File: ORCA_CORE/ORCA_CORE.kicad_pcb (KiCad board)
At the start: 2 copper layers, 69.8 x 41.9 mm, 176 parts, among them J1 data_line_power, J10 Raspberry_Pi_2_3, J11 I2C, J12 I2C, J13 6Vout, J14 5Vout, J15 Conn_01x05_Pin, J16 Conn_01x05_Pin, J17 Vin_motor, J18 data_line_power, J19 +5Vout_cpu, J2 I2C_power, J20 5Vout, J3 Vout_motor, J4 emergence, J5 Vin_batt, J6 Vin_ex, J7 Vout_power2usp, J8 Vin_power2usp, J9 +5Vout_cpu, P1 USB_C_Plug_USB2.0, Q1 TJ60S04M3L, Q2 BSS138, Q3 BSS138, Q4 IRLML6402, Q5 TJ60S04M3L, Q6 BSS138, Q7 BSS138, U1 LTC2301IMS, U10 HY2112, U11 AP64502, U12 TPS61230A__board, U13 FT230XS, U14 BNO055, U15 NJM78055DL1, U2 NJM78055DL1, U3 CN3058E, U4 RH1B-UDC6V, U5 TPH11006NL, U6 TPH11006NL, U7 NJW4860, U8 AZ1117-3.3, U9 FS8205

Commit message: plate power and usp
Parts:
- removed H7, H8: Hole_usp, MountingHole:MountingHole_3.2mm_M3
- added C51: 4.7u, Capacitor_SMD:C_0603_1608Metric_Pad1.08x0.95mm_HandSolder, B.Cu at (197.5, -40.9)
- added J21: Conn_01x02, Battery:BatteryHolder_1xAA_code, F.Cu at (162.9, -53.8)
- added ORCA_CORE: LOGO, Logo:ORCA_logo, F.Cu at (69.8, -38.7)
- added ORCA_CORE: LOGO, Logo:ORCA_logo, F.Cu at (164.7, -41.7)
- added Q8: BSS138, Package_TO_SOT_SMD:SOT-23, F.Cu at (-70.5, 60.0)
- added R5: 0, Resistor_SMD:R_0603_1608Metric_Pad0.98x0.95mm_HandSolder, F.Cu at (221.6, -43.6)
- added R6: 2.2k, Resistor_SMD:R_0603_1608Metric_Pad0.98x0.95mm_HandSolder, F.Cu at (-70.8, 63.5)
- C24, C25, C26, C27, C28, C29, C30, C31, C32, C33, C34, C35, C41, D13, D17, Q5, R21, R22, R23, R24, R25, R26, R27, R28, R29, R30, R31, R32, R33, U10, U11, U3, U9: moved to B.Cu
- J19: value +5Vout_cpu -> +5Vin_cpu
- L1: footprint Inductor_SMD:L_12x12mm_H8mm -> Inductor_SMD:L_12x12mm_H8mm_withmodel
- P1: footprint Connector_USB:USB_C_Receptacle_HCTL_HC-TYPE-C-16P-01A -> Connector_USB:USB_C_Receptacle_HCTL_HC-TYPE-C-16P-01A_withmodel
- R34: value 0 -> 2.2k
- moved U10 350.3 mm to (214.4, -58.2)
- moved U9 342.0 mm to (214.4, -53.5), turned to 180 degrees
- moved U3 337.7 mm to (165.7, -58.6), turned to 180 degrees
- moved R27 336.5 mm to (208.1, -48.1), turned to 180 degrees
- moved D18 335.1 mm to (201.3, -40.5)
- moved R30 334.8 mm to (208.5, -58.2), turned to -90 degrees
- moved H6 334.4 mm to (223.3, -59.2)
- moved D17 333.8 mm to (191.4, -46.2), turned to 180 degrees
- moved R26 333.3 mm to (211.2, -45.6), turned to 180 degrees
- moved C35 333.0 mm to (206.0, -58.2), turned to -90 degrees
- moved C25 332.4 mm to (165.7, -55.1)
- moved R25 329.4 mm to (211.2, -43.7), turned to 180 degrees
- moved R29 328.3 mm to (208.5, -53.5), turned to -90 degrees
- moved C29 328.2 mm to (207.7, -44.6), turned to -90 degrees
- moved C39 327.4 mm to (199.3, -31.7), turned to 90 degrees
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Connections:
- C25 pad 1: bat+ -> batt+
- C31 pad 1: GND -> GND1
- C31 pad 2: /usp/Vout -> reg_down_out
- C32 pad 1: GND -> GND1
- C32 pad 2: /usp/Vout -> reg_down_out
- C33 pad 1: GND -> GND1
- C33 pad 2: /usp/Vout -> reg_down_out
- C34 pad 1: GND -> GND1
- C34 pad 2: /usp/Vout -> reg_down_out
- C39 pad 1: GND -> reg_down_out
- C39 pad 2: /usp/Vout -> GND1
- C40 pad 2: GND -> GND1
- C41 pad 2: reg_up_out -> reg_down
- C42 pad 2: reg_up_out -> reg_down
- C43 pad 2: reg_up_out -> reg_down
- C44 pad 2: GND -> GND1
- C45 pad 2: GND -> GND1
- D16 pad 1: /usp/Vout -> reg_down_out
- D18 pad 1: /usp/Vout -> reg_down
- D19 pad 1: GND -> GND1
- D23 pad 1: GND -> GND1
- D24 pad 3: GND -> GND1
- D24 pad 4: full_color_led -> full_color_led_5V
- J10 pad 14: GND -> GND1
- J10 pad 20: GND -> GND1
- J10 pad 22: full_color_led -> full_color_led_3V3
- J10 pad 25: GND -> GND1
- J10 pad 30: GND -> GND1
- J10 pad 34: GND -> GND1
- J10 pad 39: GND -> GND1
- J10 pad 6: GND -> GND1
- J10 pad 9: GND -> GND1
- J14 pad 1: GND -> GND1
- J19 pad 1: GND -> GND1
- J9 pad 1: GND -> GND1
- J9 pad 2: /usp/Vout -> reg_down_out
- P1 pad A1: GND -> GND1
- P1 pad A12: GND -> GND1
- P1 pad B1: GND -> GND1
- P1 pad B12: GND -> GND1
- P1 pad S1: GND -> GND1
- R34 pad 1: GND -> +5V_cpu
- R34 pad 2: GND -> full_color_led_5V
- R39 pad 1: GND -> GND1
- U13 pad 13: GND -> GND1
- U13 pad 5: GND -> GND1
- U14 pad 2: GND -> GND1
- U14 pad 7: GND -> GND1
- U3 pad 5: bat+ -> batt+
- U3 pad 8: bat+ -> batt+
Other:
- board size 69.8 x 41.9 mm -> 169.9 x 43 mm
- board text added: "3V3"
- board text added: "5Vout"
- board text added: "I2C"
- board text added: "SCL"
- board text added: "SDA"
- board text added: "Vin"
- board text added: "batt"
- board text added: "battery"
- board text added: "charge"
- board text added: "data line"
- board text added: "emerge_detector"
- board text added: "emerge_order"
- board text added: "enable"
- board text added: "external"
- board text added: "full"
- board text added: "motor"
- board text added: "power board v1 2025/02/19"
- board text added: "power_checker"
- board text added: "usp"
- board text added: "usp board v1 2025/02/19"

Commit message: plate all parts
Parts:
- removed H11, H12: Hole_cup, MountingHole:MountingHole_3.2mm_M3
- removed J14: 5Vout, Conn:power_pad
- added ORCA_CORE: LOGO, Logo:ORCA_logo, F.Cu at (106.0, 46.4)
- added R47: 2.2k, Resistor_SMD:R_0603_1608Metric_Pad0.98x0.95mm_HandSolder, F.Cu at (118.1, 55.6)
- added R48: 2.2k, Resistor_SMD:R_0603_1608Metric_Pad0.98x0.95mm_HandSolder, F.Cu at (120.7, 55.6)
- added R49: 2.2k, Resistor_SMD:R_0603_1608Metric_Pad0.98x0.95mm_HandSolder, F.Cu at (115.6, 55.6)
- added R50: 2.2k, Resistor_SMD:R_0603_1608Metric_Pad0.98x0.95mm_HandSolder, B.Cu at (124.2, 153.3)
- C40, C44, C45, C46, C47, C48, C49, C50, D22, D25, Q6, Q7, Q8, R34, R37, R38, R39, R40, R41, R42, R43, R44, R45, R46, R6, U13, U15: moved to B.Cu
- J10: footprint Connector_PinSocket_2.54mm:PinSocket_2x20_P2.54mm_Horizontal -> cpu:raspberrypi_Zero_W_Vertical
- moved J10 273.3 mm to (153.8, 41.3), turned to -90 degrees
- moved R35 270.6 mm to (156.8, 42.8), turned to -90 degrees
- moved C47 269.4 mm to (154.9, 61.0), turned to 90 degrees
- moved C40 268.9 mm to (154.9, 45.2), turned to -90 degrees
- moved R36 267.6 mm to (156.8, 61.3), turned to 90 degrees
- moved C46 267.0 mm to (152.4, 61.0), turned to 90 degrees
- moved C45 266.2 mm to (152.3, 45.2), turned to -90 degrees
- moved D24 259.7 mm to (148.0, 63.2)
- moved J15 253.2 mm to (152.7, 49.6), turned to -90 degrees
- moved C48 248.7 mm to (157.5, 60.9), turned to 90 degrees
- moved J16 248.6 mm to (152.7, 53.4), turned to -90 degrees
- moved R40 248.5 mm to (138.4, 62.7), turned to -90 degrees
- moved C44 246.8 mm to (157.5, 45.4), turned to -90 degrees
- moved R41 246.6 mm to (137.2, 53.4), turned to -90 degrees
- moved R42 246.5 mm to (137.2, 48.3), turned to 90 degrees
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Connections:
- R41 pad 2: SDA -> SCL
- R42 pad 2: SCL -> SDA
- U14 pad 3: SCL -> SDA
- U14 pad 4: SDA -> SCL
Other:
- board size 169.9 x 43 mm -> 73 x 134.1 mm
- board text added: "12"
- board text added: "13"
- board text added: "16"
- board text added: "17"
- board text added: "18"
- board text added: "19"
- board text added: "20"
- board text added: "21"
- board text added: "26"
- board text added: "27"
- board text added: "Vin_5Vcpu"
- board text added: "cpu board v1 2025/02/19"
- board text added: "emerge sw"
- board text removed: "batt"

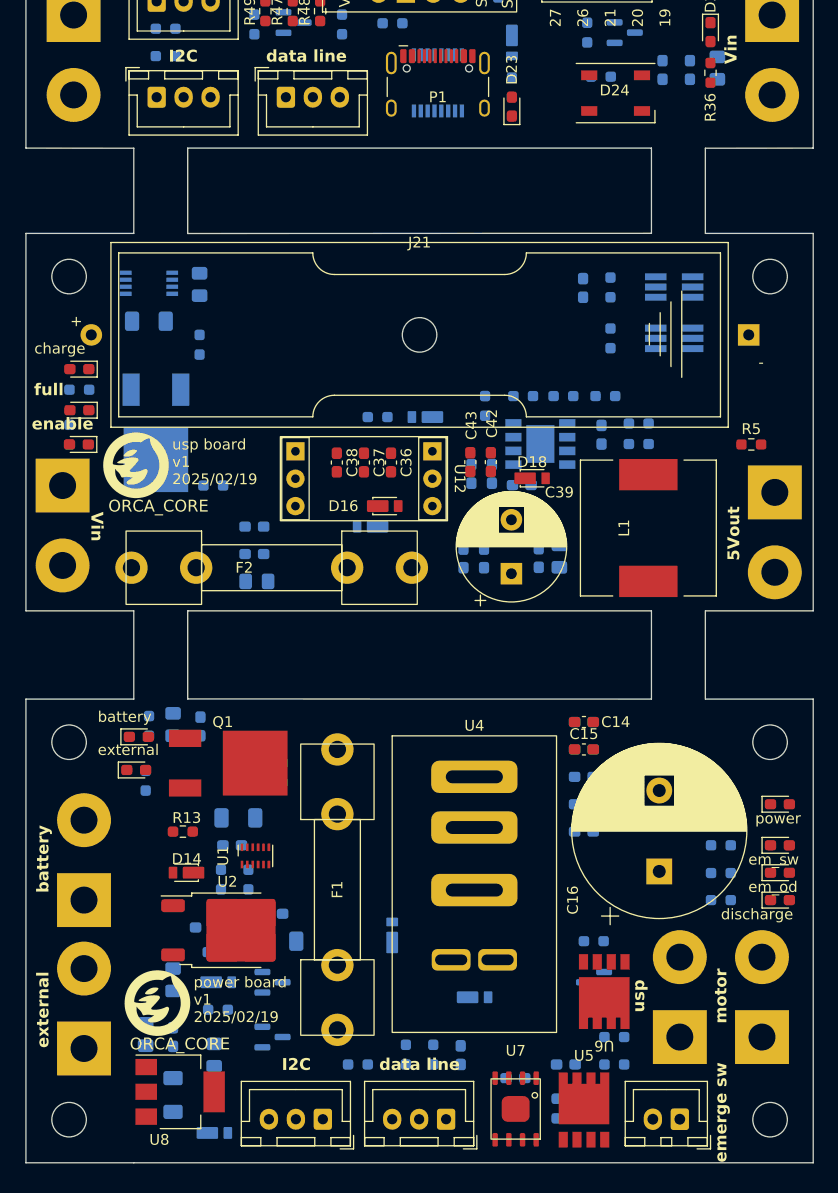
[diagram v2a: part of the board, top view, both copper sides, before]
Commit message: wire and fill power board
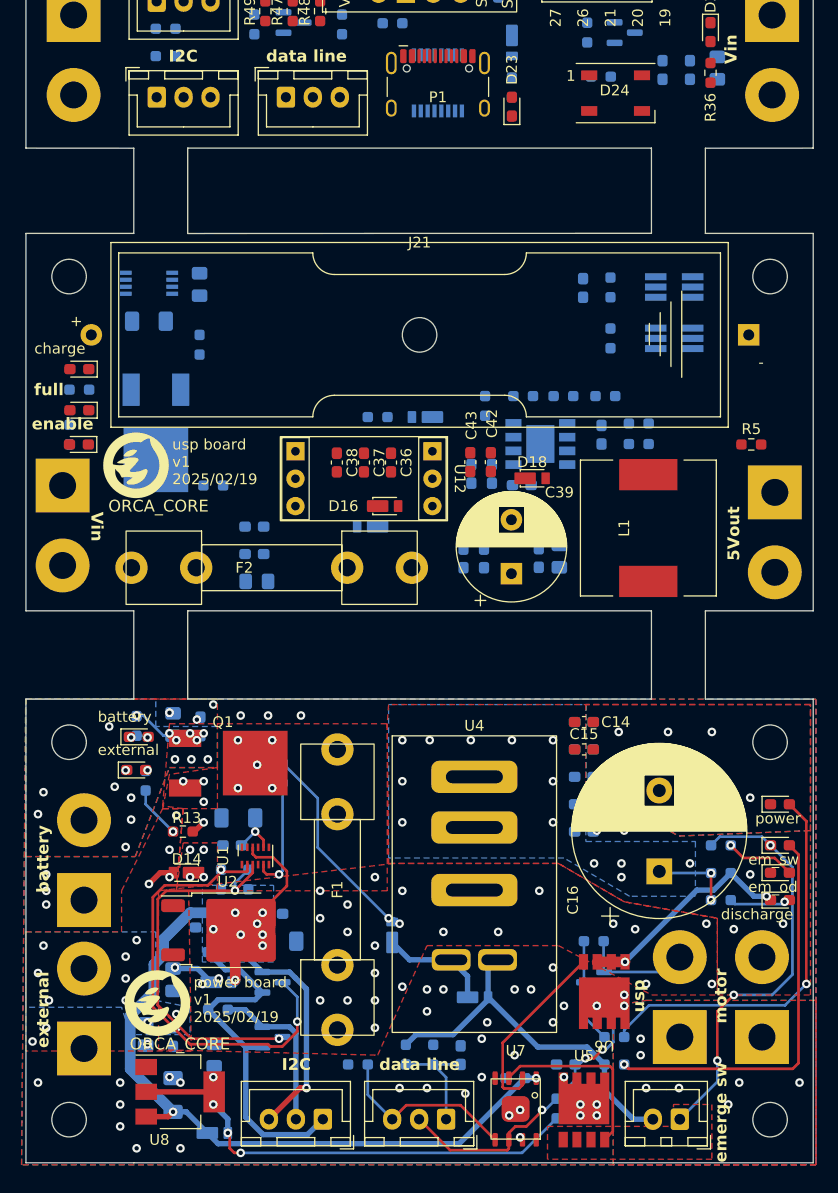
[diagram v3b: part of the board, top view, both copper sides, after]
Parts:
- moved R1 1.15 mm to (103.6, 121.9)
- turned R14 to 0 degrees
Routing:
- net +5V_power: track 0.00 -> 82.1 mm, vias 0 -> 10
- net +3V3_power: track 0.00 -> 46.4 mm, vias 0 -> 4
- net SDA_5V: track 0.00 -> 41.5 mm, vias 0 -> 2
- net Net-(D6-K): track 0.00 -> 38.8 mm, vias 0 -> 3
- net Net-(D6-A): track 0.00 -> 37.1 mm, vias 0 -> 1
- net Net-(D5-A): track 0.00 -> 36.6 mm, vias 0 -> 1
- net SCL_5V: track 0.00 -> 35.8 mm, vias 0 -> 2
- net +6V_power: track 0.00 -> 35.5 mm, vias 0 -> 26
- net Net-(D4-A): track 0.00 -> 34.8 mm
- net VBUS_power: track 0.00 -> 33.7 mm
- net /power/power_checker: track 0.00 -> 30.4 mm, vias 0 -> 3
- net /power/SDA_3V3: track 0.00 -> 22.6 mm, vias 0 -> 1
- net Net-(D8-K): track 0.00 -> 20.5 mm, vias 0 -> 2
- net /power/emerge_order: track 0.00 -> 17.4 mm
- net Net-(U7-OUTA): track 0.00 -> 17.4 mm
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- added copper zone on B.Cu, net +5V_power
- added copper zone on F.Cu, net +6V_power
- added copper zone on In1.Cu, net +6V_power
- added copper zone on B.Cu, net +BATT_power
- added copper zone on F.Cu, net +BATT_power
- added copper zone on In1.Cu, net +BATT_power
- added copper zone on B.Cu, net +VDD_power
- added copper zone on F.Cu, net +VDD_power
- added copper zone on In1.Cu, net +VDD_power
- added copper zone on B.Cu, net /power/Vout_motor
- added copper zone on F.Cu, net /power/Vout_motor
- added copper zone on In1.Cu, net /power/Vout_motor
- added copper zone on B.Cu, net GND
- added copper zone on F.Cu, net GND
- added copper zone on In1.Cu, net GND
- added copper zone on In2.Cu, net GND
- added copper zone on F.Cu, net Net-(D14-K)
- added copper zone on In1.Cu, net Net-(D14-K)
- added copper zone on F.Cu, net Net-(D6-K)
- added copper zone on In2.Cu, net Net-(Q1-G)
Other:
- copper layers 2 -> 4

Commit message: wiring and filling power complete
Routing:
- net GND: track 0.68 -> 9.18 mm, vias 65 -> 75
- net +VDD_power: track 7.53 -> 10.2 mm, vias 17 -> 14
- net Net-(D6-K): track 38.8 -> 41.3 mm
- net Net-(D14-K): track 0.00 -> 2.26 mm
- net Net-(U7-OUTB): track 17.1 -> 16.0 mm, vias 0 -> 2
- net Net-(D5-A): track 36.6 -> 37.5 mm
- net /power/power_checker: track 30.4 -> 31.2 mm
- net +5V_power: track 82.1 -> 82.7 mm, vias 10 -> 12
- net Net-(D8-K): track 20.5 -> 20.7 mm, vias 2 -> 3
- net Net-(D6-A): vias 1 -> 2
- net Net-(D8-A): vias 1 -> 2
- net /power/Vout_motor: vias 18 -> 27
- net +6V_power: vias 26 -> 33
- added copper zone on B.Cu, net +6V_power

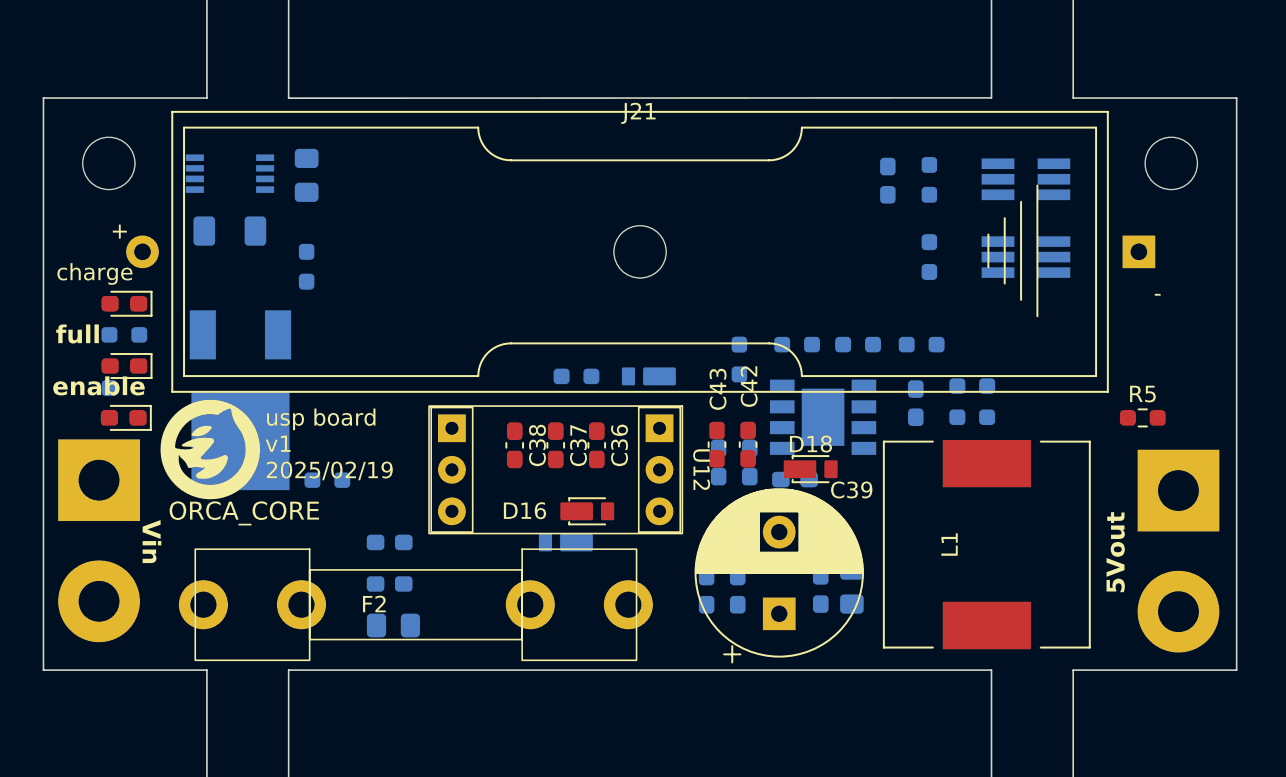
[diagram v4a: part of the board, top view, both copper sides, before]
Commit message: complete wireing and filling usp
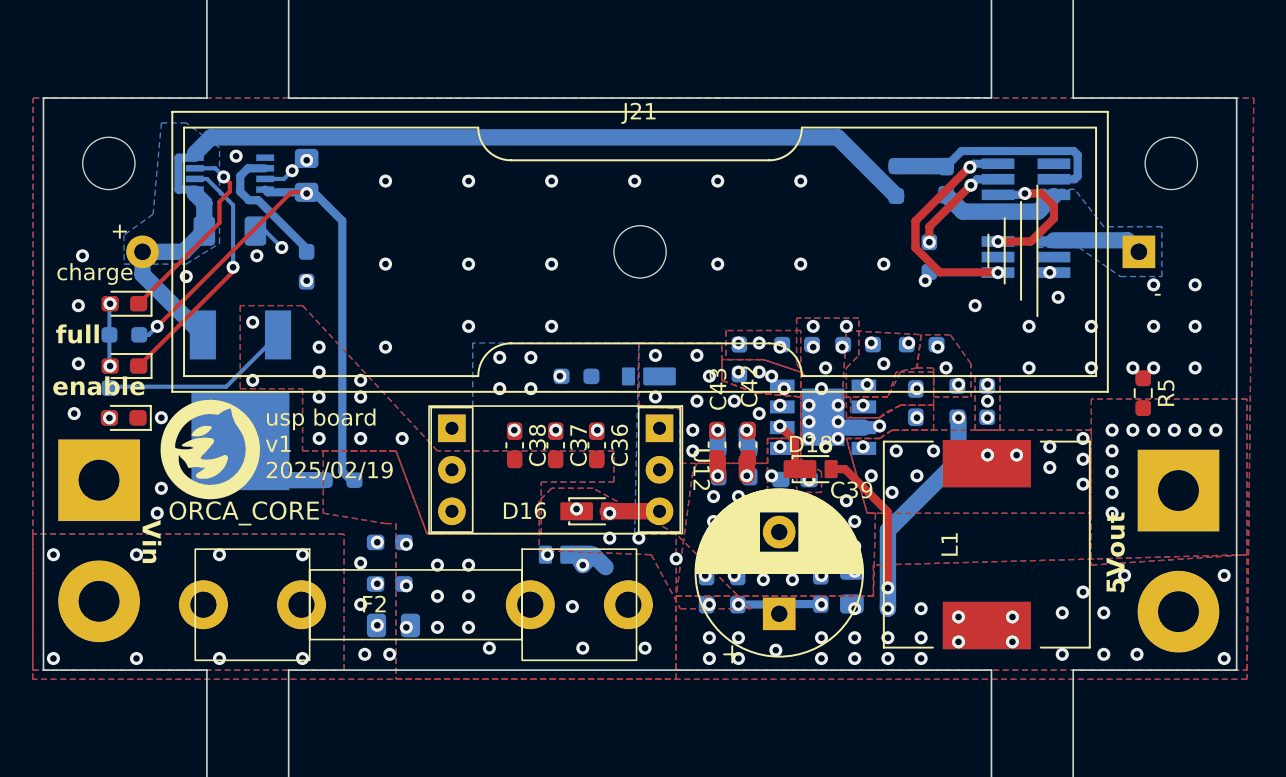
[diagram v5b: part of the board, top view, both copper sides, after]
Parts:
- moved C35 3.56 mm to (148.6, 81.3)
- moved R30 2.03 mm to (145.5, 81.3)
- moved R5 1.51 mm to (160.7, 94.3), turned to -90 degrees
- moved D13 0.75 mm to (125.3, 104.1)
- moved R33 0.74 mm to (111.5, 99.6)
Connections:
- C31 pad 1: GND1 -> GND
- C32 pad 1: GND1 -> GND
- C33 pad 1: GND1 -> GND
- C34 pad 1: GND1 -> GND
- C39 pad 2: GND1 -> GND
- C40 pad 2: GND1 -> GND2
- C44 pad 2: GND1 -> GND2
- C45 pad 2: GND1 -> GND2
- D19 pad 1: GND1 -> GND2
- D23 pad 1: GND1 -> GND2
- D24 pad 3: GND1 -> GND2
- J10 pad 14: GND1 -> GND2
- J10 pad 20: GND1 -> GND2
- J10 pad 25: GND1 -> GND2
- J10 pad 30: GND1 -> GND2
- J10 pad 34: GND1 -> GND2
- J10 pad 39: GND1 -> GND2
- J10 pad 6: GND1 -> GND2
- J10 pad 9: GND1 -> GND2
- J19 pad 1: GND1 -> GND2
- P1 pad A1: GND1 -> GND2
- P1 pad A12: GND1 -> GND2
- P1 pad B1: GND1 -> GND2
- P1 pad B12: GND1 -> GND2
- P1 pad S1: GND1 -> GND2
- R39 pad 1: GND1 -> GND2
- R47 pad 2: GND1 -> GND2
- R48 pad 2: GND1 -> GND2
- R49 pad 2: GND1 -> GND2
- U13 pad 13: GND1 -> GND2
- U13 pad 5: GND1 -> GND2
- U14 pad 2: GND1 -> GND2
- U14 pad 7: GND1 -> GND2
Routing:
- net batt+: track 0.00 -> 62.2 mm
- net reg_down_out: track 0.00 -> 41.2 mm, vias 0 -> 38
- net +VDD_usp: track 0.00 -> 38.4 mm, vias 0 -> 20
- net GND: track 9.18 -> 41.2 mm, vias 75 -> 166
- net Net-(D12-K): track 0.00 -> 15.2 mm, vias 0 -> 1
- net Net-(U10-VDD): track 0.00 -> 14.4 mm
- net Net-(U10-OC): track 0.00 -> 13.8 mm, vias 0 -> 2
- net batt-: track 0.00 -> 12.9 mm
- net Net-(D10-K): track 0.00 -> 12.2 mm, vias 0 -> 1
- net reg_up: track 0.00 -> 11.7 mm, vias 0 -> 10
- net Net-(U10-OD): track 0.00 -> 8.54 mm, vias 0 -> 2
- net Net-(U3-ISET): track 0.00 -> 8.37 mm
- net Net-(U10-CS): track 0.00 -> 6.34 mm, vias 0 -> 2
- net reg_up_out: track 0.00 -> 6.27 mm, vias 0 -> 1
- net Net-(Q5-G): track 0.00 -> 6.14 mm
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- added copper zone on B.Cu, net +VDD_usp
- added copper zone on F.Cu, net +VDD_usp
- added copper zone on In1.Cu, net +VDD_usp
- added copper zone on B.Cu, net /usp/Vin
- added copper zone on F.Cu, net /usp/Vin
- added copper zone on In1.Cu, net /usp/Vin
- added copper zone on In2.Cu, net /usp/Vin
- added copper zone on B.Cu, net GND1
- added copper zone on F.Cu, net GND1
- added copper zone on In1.Cu, net GND1
- added copper zone on In2.Cu, net GND1
- added copper zone on B.Cu, net Net-(R23-Pad2)
- added copper zone on F.Cu, net Net-(R23-Pad2)
- added copper zone on In1.Cu, net Net-(R23-Pad2)
- added copper zone on In2.Cu, net Net-(R23-Pad2)
- added copper zone on B.Cu, net Net-(R25-Pad1)
- added copper zone on F.Cu, net Net-(R25-Pad1)
- added copper zone on In1.Cu, net Net-(R25-Pad1)
- added copper zone on In2.Cu, net Net-(R25-Pad1)
- added copper zone on B.Cu, net Net-(R26-Pad2)
- added copper zone on F.Cu, net Net-(R26-Pad2)
- added copper zone on In1.Cu, net Net-(R26-Pad2)
- added copper zone on In2.Cu, net Net-(R26-Pad2)
- added copper zone on B.Cu, net Net-(U11-BST)
- added copper zone on F.Cu, net Net-(U11-BST)
- added copper zone on In1.Cu, net Net-(U11-BST)
- added copper zone on In2.Cu, net Net-(U11-BST)
- added copper zone on B.Cu, net Net-(U11-FB)
- added copper zone on F.Cu, net Net-(U11-FB)
- added copper zone on In1.Cu, net Net-(U11-FB)
- added copper zone on In2.Cu, net Net-(U11-FB)
- added copper zone on B.Cu, net Net-(U11-RT/CLK)
- added copper zone on F.Cu, net Net-(U11-RT/CLK)
- added copper zone on In1.Cu, net Net-(U11-RT/CLK)
- added copper zone on In2.Cu, net Net-(U11-RT/CLK)
- added copper zone on B.Cu, net Net-(U11-SS)
- added copper zone on F.Cu, net Net-(U11-SS)
- added copper zone on In1.Cu, net Net-(U11-SS)
- added copper zone on In2.Cu, net Net-(U11-SS)
- added copper zone on B.Cu, net Net-(U11-SW)
- added copper zone on F.Cu, net Net-(U11-SW)
- added copper zone on In1.Cu, net Net-(U11-SW)
- added copper zone on In2.Cu, net Net-(U11-SW)
- added copper zone on B.Cu, net batt+
- added copper zone on B.Cu, net batt-
- added copper zone on B.Cu, net reg_down
- added copper zone on F.Cu, net reg_down
- added copper zone on In1.Cu, net reg_down
- added copper zone on In2.Cu, net reg_down
- added copper zone on B.Cu, net reg_down_out
- added copper zone on F.Cu, net reg_down_out
- added copper zone on In1.Cu, net reg_down_out
- added copper zone on In2.Cu, net reg_down_out
- added copper zone on B.Cu, net reg_up
- added copper zone on F.Cu, net reg_up
- added copper zone on In1.Cu, net reg_up
